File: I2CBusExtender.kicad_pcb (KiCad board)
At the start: 2 copper layers, 57.5 x 17.9 mm, 19 parts, among them J1 SBusConn, J2 LBusCon, U1 P82B715

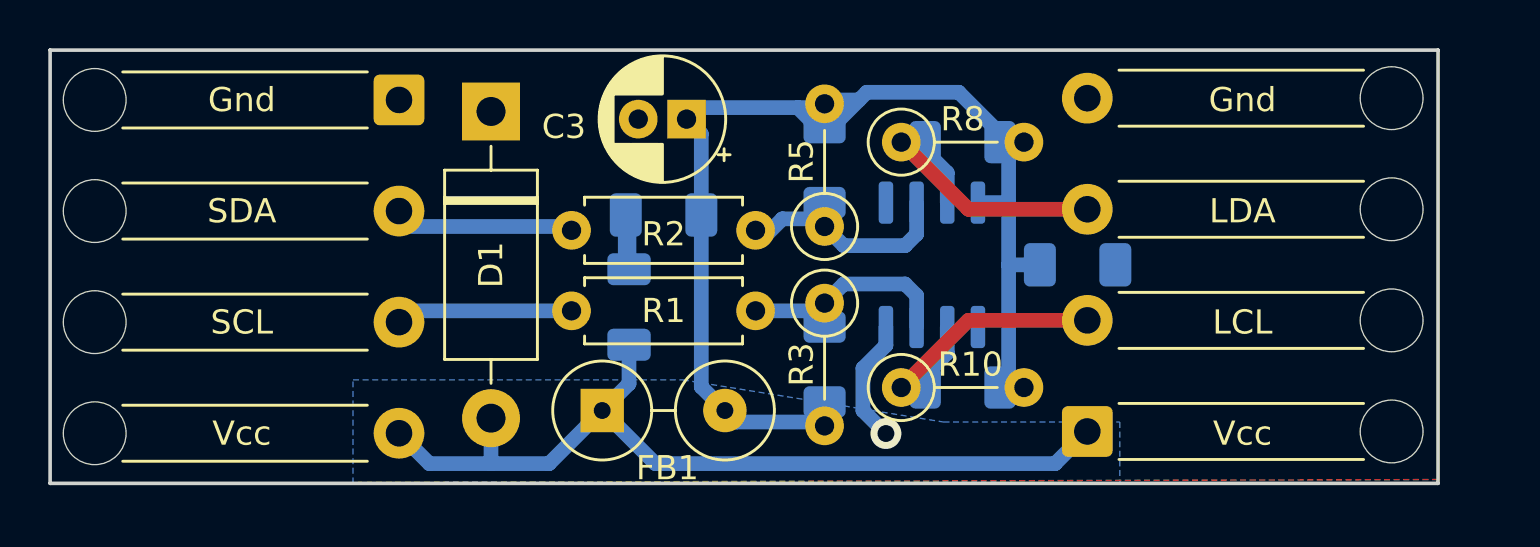
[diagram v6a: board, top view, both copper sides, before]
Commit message: Tweaked spaces between components and improved track layout.
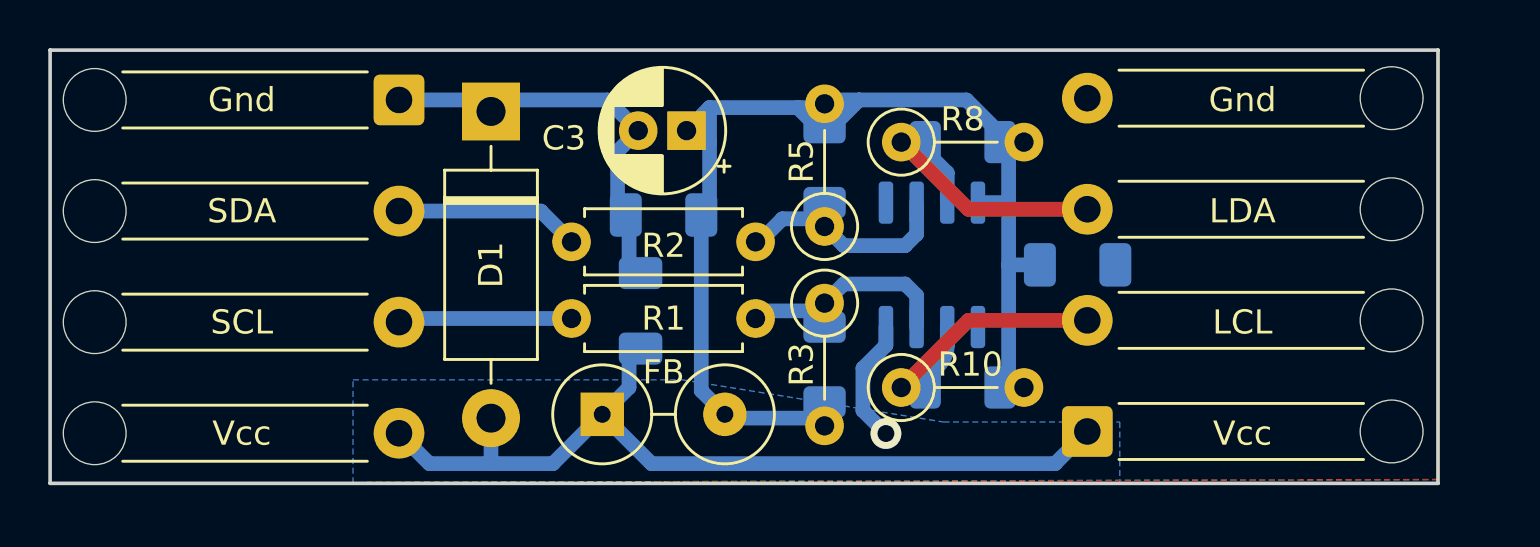
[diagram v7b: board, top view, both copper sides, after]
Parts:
- moved C1 0.50 mm to (97.9, 88.1)
- moved R2 0.48 mm to (102.7, 85.2)
- moved C3 0.48 mm to (99.9, 80.6)
- moved R1 0.32 mm to (102.7, 88.4)
- moved FB 0.16 mm to (96.4, 92.4)
- renumbered FB1 to FB
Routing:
- net /Gnd: track 9.49 -> 20.2 mm
- net /VCC: track 45.9 -> 48.2 mm
- net Net-(J2-Pad2): track 12.7 -> 11.4 mm
- net Net-(J1-Pad3): track 7.61 -> 6.83 mm
- net Net-(J1-Pad2): track 7.14 -> 7.67 mm

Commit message: Tweaked track layout.
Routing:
- net /Gnd: track 20.2 -> 22.0 mm
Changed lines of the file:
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@@
   (segment (start 91.7575 92.55125) (end 91.7575 94.4325) (width 0.6096) (layer "B.Cu") (net 3))
   (via (at 108.10875 93.18625) (size 1.28) (drill 0.7) (layers "F.Cu" "B.Cu") (net 4))
+  (segment (start 96.99625 79.7875) (end 96.99625 81.5025) (width 0.6096) (layer "B.Cu") (net 4))
+  (segment (start 108.10875 88.77625) (end 108.10875 89.535) (width 0.6096) (layer "B.Cu") (net 4))
   (segment (start 92.86875 79.375) (end 96.58375 79.375) (width 0.6096) (layer "B.Cu") (net 4))
-  (segment (start 108.10875 88.77625) (end 108.10875 89.535) (width 0.6096) (layer "B.Cu") (net 4))
-  (segment (start 96.58375 79.375) (end 97.85375 80.645) (width 0.6096) (layer "B.Cu") (net 4))
-  (segment (start 97.85375 80.645) (end 96.99625 81.5025) (width 0.6096) (layer "B.Cu") (net 4))
   (segment (start 108.10875 89.535) (end 107.15625 90.4875) (width 0.6096) (layer "B.Cu") (net 4))
   (segment (start 91.28125 79.375) (end 91.7575 79.85125) (width 0.6096) (layer "B.Cu") (net 4))
-  (segment (start 96.99625 81.5025) (end 96.99625 83.66125) (width 0.6096) (layer "B.Cu") (net 4))
+  (segment (start 96.99625 81.5025) (end 96.99625 83.795) (width 0.6096) (layer "B.Cu") (net 4))
   (segment (start 107.15625 92.23375) (end 108.10875 93.18625) (width 0.6096) (layer "B.Cu") (net 4))
   (segment (start 107.15625 90.4875) (end 107.15625 92.23375) (width 0.6096) (layer "B.Cu") (net 4))
   (segment (start 87.9475 79.375) (end 91.28125 79.375) (width 0.6096) (layer "B.Cu") (net 4))
+  (segment (start 97.85375 80.645) (end 96.99625 81.5025) (width 0.6096) (layer "B.Cu") (net 4))
+  (segment (start 96.58375 79.375) (end 96.99625 79.7875) (width 0.6096) (layer "B.Cu") (net 4))
+  (segment (start 96.99625 79.7875) (end 97.85375 80.645) (width 0.6096) (layer "B.Cu") (net 4))
   (segment (start 97.4725 86.54375) (end 97.4725 84.455) (width 0.6096) (layer "B.Cu") (net 4))
   (segment (start 93.8175 83.975) (end 95.09125 85.24875) (width 0.6096) (layer "B.Cu") (net 5))
